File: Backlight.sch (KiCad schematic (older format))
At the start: 83 parts, among them J9 LED_DATA, Q2 Q_NMOS_GSD

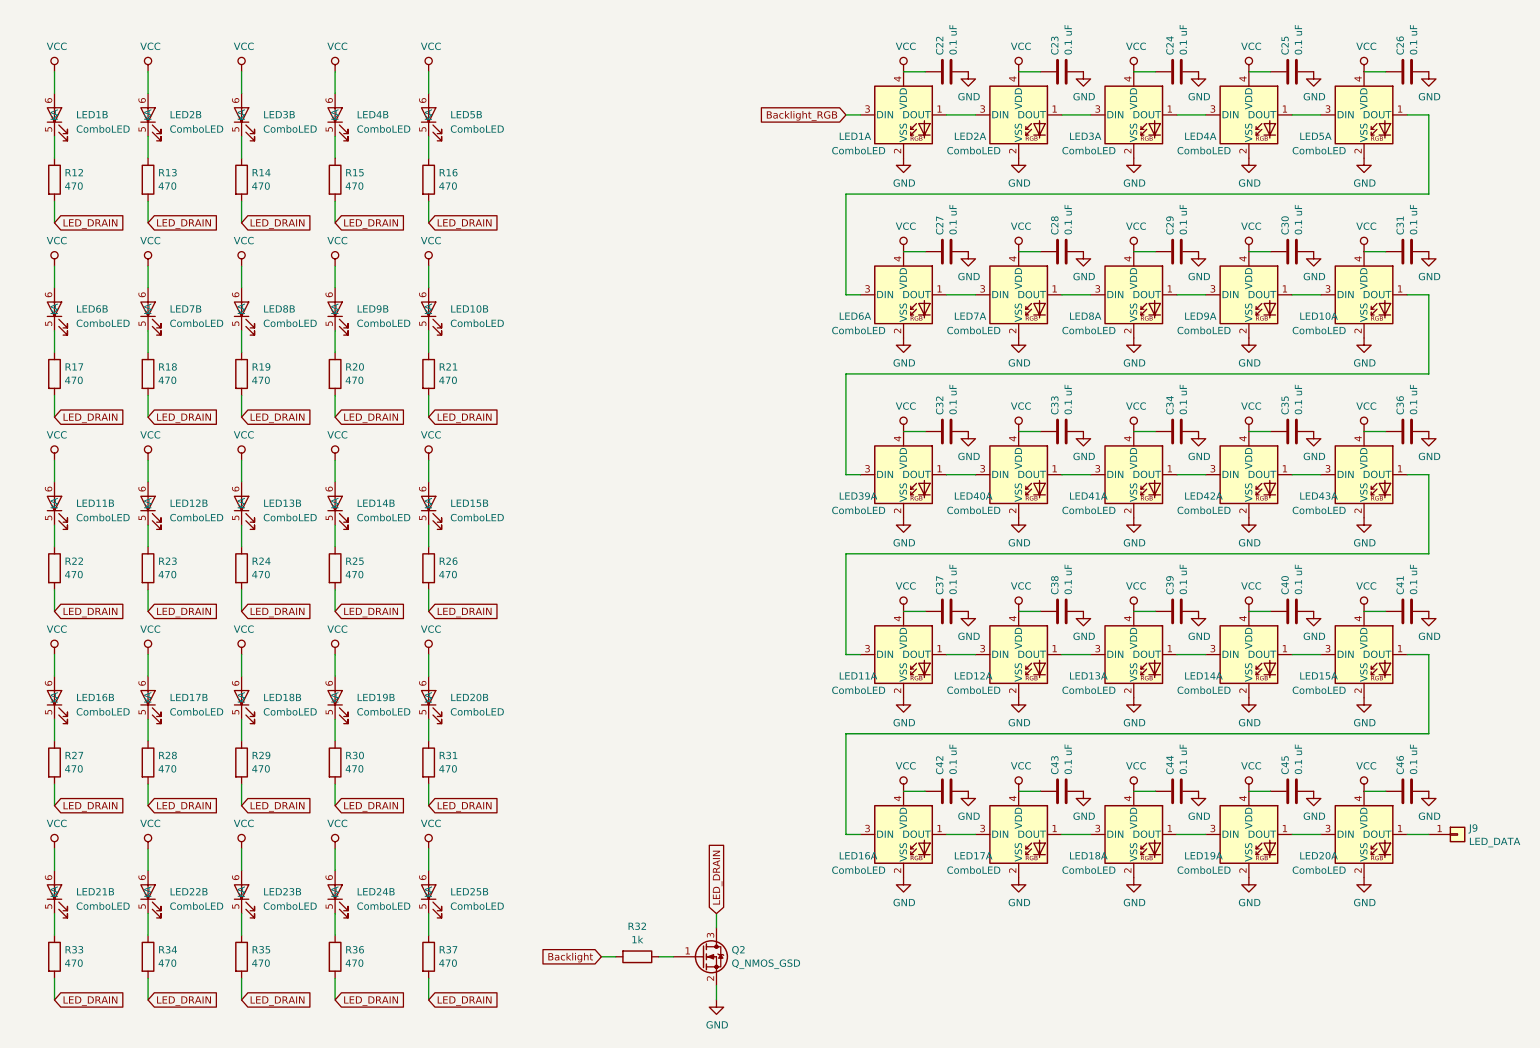
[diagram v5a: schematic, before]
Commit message: initial pcb layout and schematic optimizations
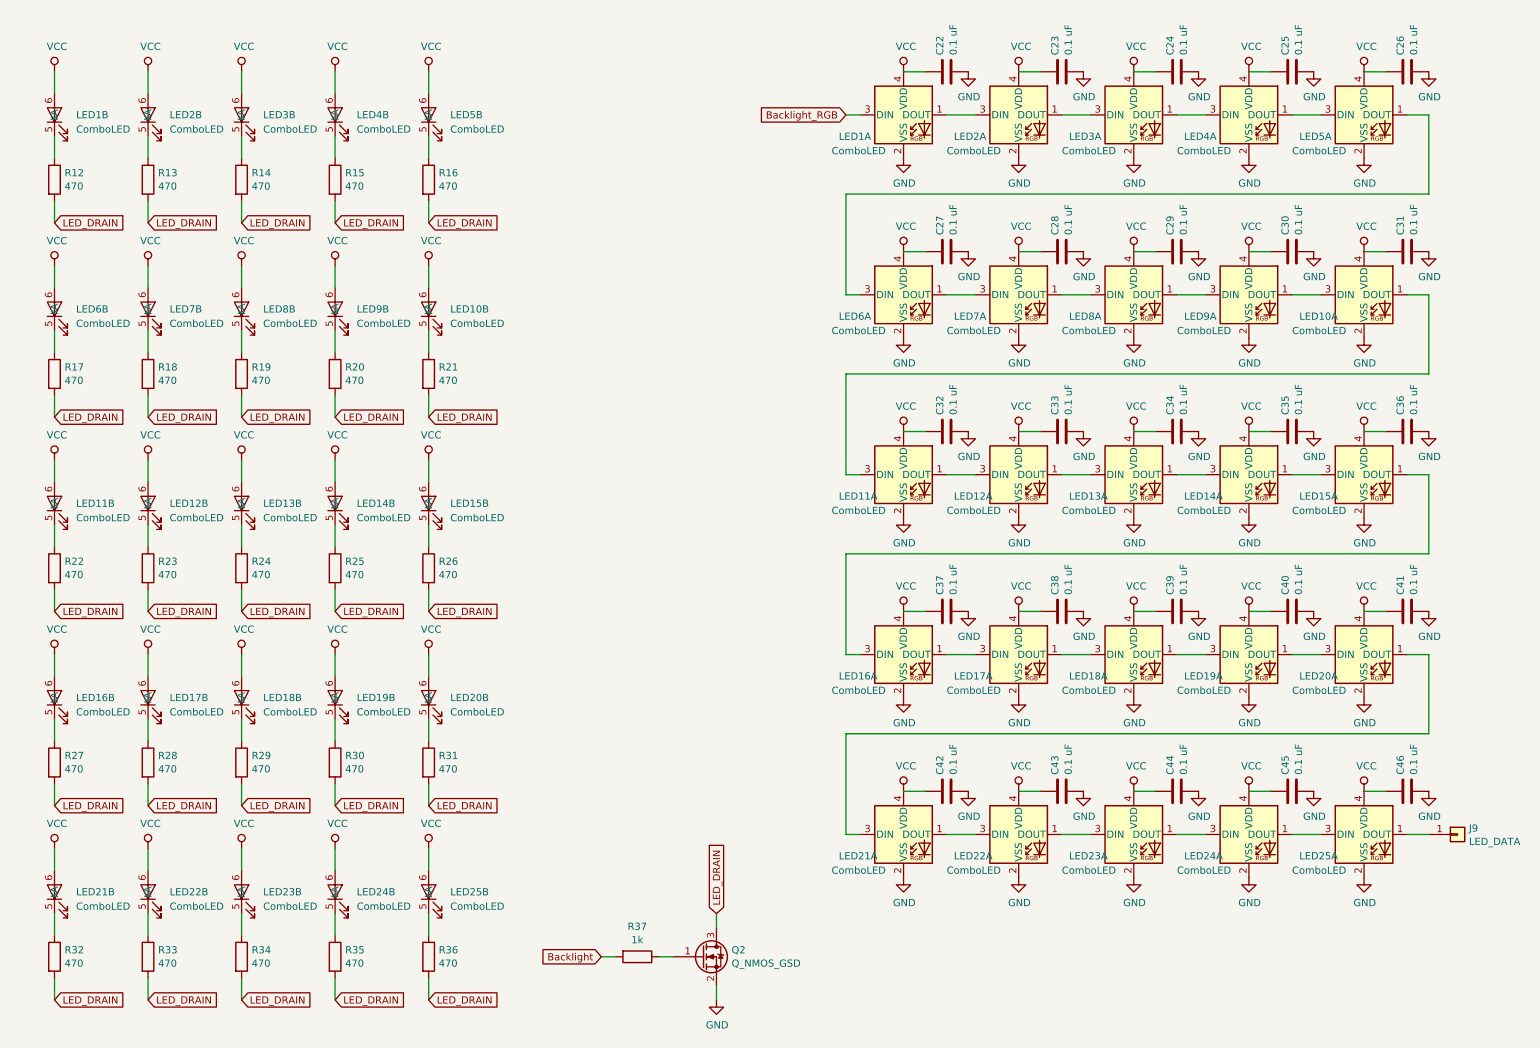
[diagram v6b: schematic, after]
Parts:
- renumbered LED39 to LED11, LED40 to LED12, LED41 to LED13, LED42 to LED14, LED43 to LED15, LED11 to LED16, LED12 to LED17, LED13 to LED18, LED14 to LED19, LED15 to LED20, LED16 to LED21, LED17 to LED22, LED18 to LED23, LED19 to LED24, LED20 to LED25, R33 to R32, R34 to R33, R35 to R34, R36 to R35, R37 to R36, R32 to R37
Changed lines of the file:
@@
 P 4850 7050
 AR Path="/5D7A2731" Ref="R?"  Part="1"
-AR Path="/5D79FC99/5D7A2731" Ref="R32"  Part="1"
-F 0 "R32" V 4640 7050 50  0000 C CNN
+AR Path="/5D79FC99/5D7A2731" Ref="R37"  Part="1"
+F 0 "R37" V 4640 7050 50  0000 C CNN
 F 1 "1k" V 4733 7050 50  0000 C CNN
 F 2 "Resistor_SMD:R_0805_2012Metric" V 4780 7050 50  0001 C CNN
@@
 $EndComp
 $Comp
-L Device:R R33
+L Device:R R32
 U 1 1 5D7D110F
 P 800 7050
-F 0 "R33" H 870 7097 50  0000 L CNN
+F 0 "R32" H 870 7097 50  0000 L CNN
 F 1 "470" H 870 7004 50  0000 L CNN
 F 2 "Resistor_SMD:R_0805_2012Metric" V 730 7050 50  0001 C CNN
@@
 LED_DRAIN
 $Comp
-L Device:R R34
+L Device:R R33
 U 1 1 5D7D111F
 P 1450 7050
-F 0 "R34" H 1520 7097 50  0000 L CNN
+F 0 "R33" H 1520 7097 50  0000 L CNN
 F 1 "470" H 1520 7004 50  0000 L CNN
 F 2 "Resistor_SMD:R_0805_2012Metric" V 1380 7050 50  0001 C CNN
@@
 $EndComp
 $Comp
-L Device:R R35
+L Device:R R34
 U 1 1 5D7D1135
 P 2100 7050
-F 0 "R35" H 2170 7097 50  0000 L CNN
+F 0 "R34" H 2170 7097 50  0000 L CNN
 F 1 "470" H 2170 7004 50  0000 L CNN
 F 2 "Resistor_SMD:R_0805_2012Metric" V 2030 7050 50  0001 C CNN
@@
 LED_DRAIN
 $Comp
-L Device:R R36
+L Device:R R35
 U 1 1 5D7D1145
 P 2750 7050
-F 0 "R36" H 2820 7097 50  0000 L CNN
+F 0 "R35" H 2820 7097 50  0000 L CNN
 F 1 "470" H 2820 7004 50  0000 L CNN
 F 2 "Resistor_SMD:R_0805_2012Metric" V 2680 7050 50  0001 C CNN
@@
 $EndComp
 $Comp
-L Device:R R37
+L Device:R R36
 U 1 1 5D7D115B
 P 3400 7050
-F 0 "R37" H 3470 7097 50  0000 L CNN
+F 0 "R36" H 3470 7097 50  0000 L CNN
 F 1 "470" H 3470 7004 50  0000 L CNN
 F 2 "Resistor_SMD:R_0805_2012Metric" V 3330 7050 50  0001 C CNN
@@
 	6300 3700 6300 3000
 $Comp
-L testatur:LED_combined_SK6812MINI_0805 LED39
+L testatur:LED_combined_SK6812MINI_0805 LED11
 U 1 1 5D8E7F4B
 P 6700 3700
-F 0 "LED39" H 6250 3550 50  0000 L CNN
+F 0 "LED11" H 6250 3550 50  0000 L CNN
 F 1 "ComboLED" H 6200 3450 50  0000 L CNN
 F 2 "testatur:LED_combined_SK6812MINI_0805" H 7250 3400 50  0001 C CNN
@@
 	9400 3700 9600 3700
 $Comp
-L testatur:LED_combined_SK6812MINI_0805 LED40
+L testatur:LED_combined_SK6812MINI_0805 LED12
 U 1 1 5D8E7F55
 P 7500 3700
-F 0 "LED40" H 7050 3550 50  0000 L CNN
+F 0 "LED12" H 7050 3550 50  0000 L CNN
 F 1 "ComboLED" H 7000 3450 50  0000 L CNN
 F 2 "testatur:LED_combined_SK6812MINI_0805" H 8050 3400 50  0001 C CNN
@@
 $EndComp
 $Comp
-L testatur:LED_combined_SK6812MINI_0805 LED41
+L testatur:LED_combined_SK6812MINI_0805 LED13
 U 1 1 5D8E7F5B
 P 8300 3700
-F 0 "LED41" H 7850 3550 50  0000 L CNN
+F 0 "LED13" H 7850 3550 50  0000 L CNN
 F 1 "ComboLED" H 7800 3450 50  0000 L CNN
 F 2 "testatur:LED_combined_SK6812MINI_0805" H 8850 3400 50  0001 C CNN
@@
 $EndComp
 $Comp
-L testatur:LED_combined_SK6812MINI_0805 LED42
+L testatur:LED_combined_SK6812MINI_0805 LED14
 U 1 1 5D8E7F61
 P 9100 3700
-F 0 "LED42" H 8650 3550 50  0000 L CNN
+F 0 "LED14" H 8650 3550 50  0000 L CNN
 F 1 "ComboLED" H 8600 3450 50  0000 L CNN
 F 2 "testatur:LED_combined_SK6812MINI_0805" H 9650 3400 50  0001 C CNN
@@
 $EndComp
 $Comp
-L testatur:LED_combined_SK6812MINI_0805 LED43
+L testatur:LED_combined_SK6812MINI_0805 LED15
 U 1 1 5D8E7F67
 P 9900 3700
-F 0 "LED43" H 9450 3550 50  0000 L CNN
+F 0 "LED15" H 9450 3550 50  0000 L CNN
 F 1 "ComboLED" H 9400 3450 50  0000 L CNN
 F 2 "testatur:LED_combined_SK6812MINI_0805" H 10450 3400 50  0001 C CNN
@@
 	6300 4950 6300 4250
 $Comp
-L testatur:LED_combined_SK6812MINI_0805 LED11
+L testatur:LED_combined_SK6812MINI_0805 LED16
 U 1 1 5D8EF85B
 P 6700 4950
-F 0 "LED11" H 6250 4800 50  0000 L CNN
+F 0 "LED16" H 6250 4800 50  0000 L CNN
 F 1 "ComboLED" H 6200 4700 50  0000 L CNN
 F 2 "testatur:LED_combined_SK6812MINI_0805" H 7250 4650 50  0001 C CNN
@@
 	9400 4950 9600 4950
 $Comp
-L testatur:LED_combined_SK6812MINI_0805 LED12
+L testatur:LED_combined_SK6812MINI_0805 LED17
 U 1 1 5D8EF865
 P 7500 4950
-F 0 "LED12" H 7050 4800 50  0000 L CNN
+F 0 "LED17" H 7050 4800 50  0000 L CNN
 F 1 "ComboLED" H 7000 4700 50  0000 L CNN
 F 2 "testatur:LED_combined_SK6812MINI_0805" H 8050 4650 50  0001 C CNN
@@
 $EndComp
 $Comp
-L testatur:LED_combined_SK6812MINI_0805 LED13
+L testatur:LED_combined_SK6812MINI_0805 LED18
 U 1 1 5D8EF86B
 P 8300 4950
-F 0 "LED13" H 7850 4800 50  0000 L CNN
+F 0 "LED18" H 7850 4800 50  0000 L CNN
 F 1 "ComboLED" H 7800 4700 50  0000 L CNN
 F 2 "testatur:LED_combined_SK6812MINI_0805" H 8850 4650 50  0001 C CNN
@@
 $EndComp
 $Comp
-L testatur:LED_combined_SK6812MINI_0805 LED14
+L testatur:LED_combined_SK6812MINI_0805 LED19
 U 1 1 5D8EF871
 P 9100 4950
-F 0 "LED14" H 8650 4800 50  0000 L CNN
+F 0 "LED19" H 8650 4800 50  0000 L CNN
 F 1 "ComboLED" H 8600 4700 50  0000 L CNN
 F 2 "testatur:LED_combined_SK6812MINI_0805" H 9650 4650 50  0001 C CNN
@@
 $EndComp
 $Comp
-L testatur:LED_combined_SK6812MINI_0805 LED15
+L testatur:LED_combined_SK6812MINI_0805 LED20
 U 1 1 5D8EF877
 P 9900 4950
-F 0 "LED15" H 9450 4800 50  0000 L CNN
+F 0 "LED20" H 9450 4800 50  0000 L CNN
 F 1 "ComboLED" H 9400 4700 50  0000 L CNN
 F 2 "testatur:LED_combined_SK6812MINI_0805" H 10450 4650 50  0001 C CNN
@@
 	6300 6200 6300 5500
 $Comp
-L testatur:LED_combined_SK6812MINI_0805 LED16
+L testatur:LED_combined_SK6812MINI_0805 LED21
 U 1 1 5D8FB416
 P 6700 6200
-F 0 "LED16" H 6250 6050 50  0000 L CNN
+F 0 "LED21" H 6250 6050 50  0000 L CNN
 F 1 "ComboLED" H 6200 5950 50  0000 L CNN
 F 2 "testatur:LED_combined_SK6812MINI_0805" H 7250 5900 50  0001 C CNN
@@
 	9400 6200 9600 6200
 $Comp
-L testatur:LED_combined_SK6812MINI_0805 LED17
+L testatur:LED_combined_SK6812MINI_0805 LED22
 U 1 1 5D8FB420
 P 7500 6200
-F 0 "LED17" H 7050 6050 50  0000 L CNN
+F 0 "LED22" H 7050 6050 50  0000 L CNN
 F 1 "ComboLED" H 7000 5950 50  0000 L CNN
 F 2 "testatur:LED_combined_SK6812MINI_0805" H 8050 5900 50  0001 C CNN
@@
 $EndComp
 $Comp
-L testatur:LED_combined_SK6812MINI_0805 LED18
+L testatur:LED_combined_SK6812MINI_0805 LED23
 U 1 1 5D8FB426
 P 8300 6200
-F 0 "LED18" H 7850 6050 50  0000 L CNN
+F 0 "LED23" H 7850 6050 50  0000 L CNN
 F 1 "ComboLED" H 7800 5950 50  0000 L CNN
 F 2 "testatur:LED_combined_SK6812MINI_0805" H 8850 5900 50  0001 C CNN
@@
 $EndComp
 $Comp
-L testatur:LED_combined_SK6812MINI_0805 LED19
+L testatur:LED_combined_SK6812MINI_0805 LED24
 U 1 1 5D8FB42C
 P 9100 6200
-F 0 "LED19" H 8650 6050 50  0000 L CNN
+F 0 "LED24" H 8650 6050 50  0000 L CNN
 F 1 "ComboLED" H 8600 5950 50  0000 L CNN
 F 2 "testatur:LED_combined_SK6812MINI_0805" H 9650 5900 50  0001 C CNN
@@
 $EndComp
 $Comp
-L testatur:LED_combined_SK6812MINI_0805 LED20
+L testatur:LED_combined_SK6812MINI_0805 LED25
 U 1 1 5D8FB432
 P 9900 6200
-F 0 "LED20" H 9450 6050 50  0000 L CNN
+F 0 "LED25" H 9450 6050 50  0000 L CNN
 F 1 "ComboLED" H 9400 5950 50  0000 L CNN
 F 2 "testatur:LED_combined_SK6812MINI_0805" H 10450 5900 50  0001 C CNN
